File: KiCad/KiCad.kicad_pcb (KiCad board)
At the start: 2 copper layers, 74.9 x 58.4 mm, 16 parts, among them M1 Servo (SG90), U1 ESP32-DEVKITC, U2 microSD-DIP-KIT

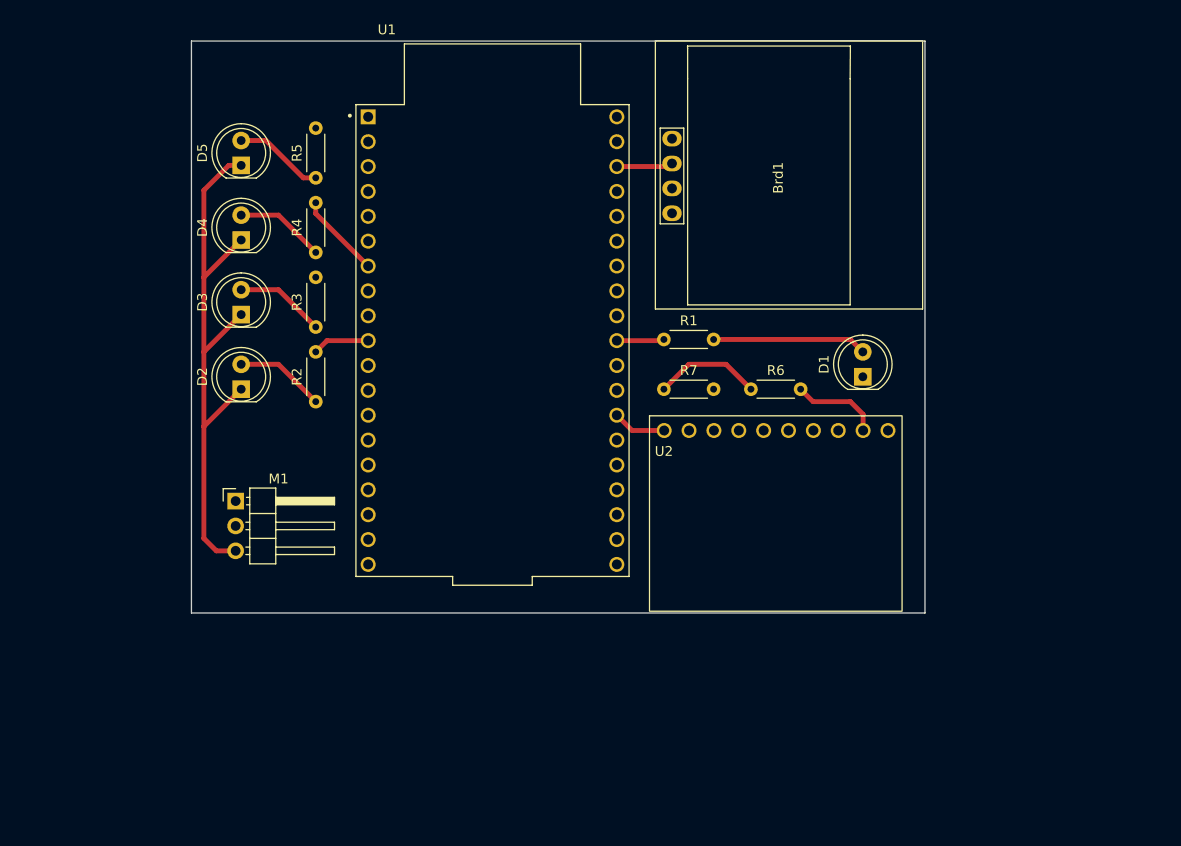
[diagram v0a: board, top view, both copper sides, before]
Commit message: KiCadの回路図追加
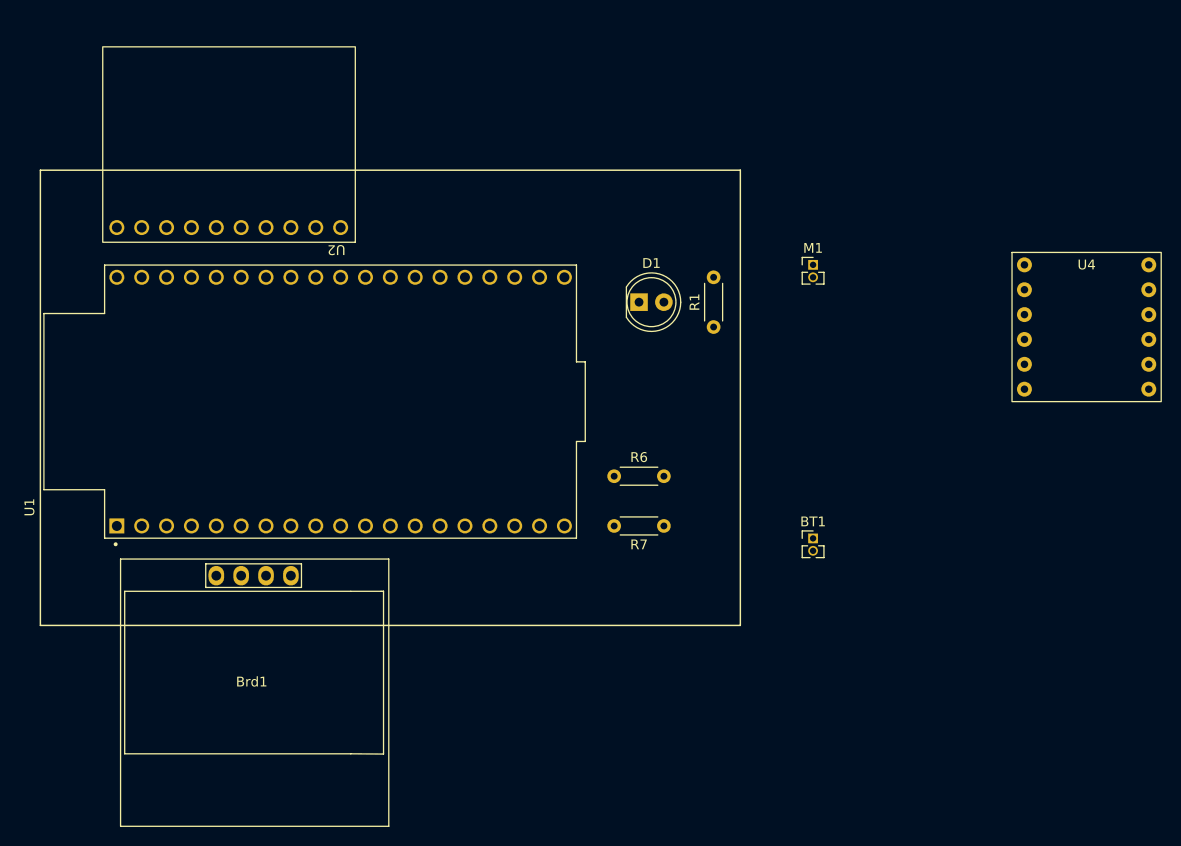
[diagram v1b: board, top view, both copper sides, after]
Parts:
- removed D2, D3, D4, D5: LED, LED_THT:LED_D5.0mm
- removed R2, R3, R4, R5: 330, Resistor_THT:R_Axial_DIN0204_L3.6mm_D1.6mm_P5.08mm_Horizontal
- added BT1: 3V (1.5V x 2), Connector_PinHeader_1.27mm:PinHeader_1x02_P1.27mm_Vertical, F.Cu at (157.5, 108.0)
- added U4: BD65496MUV, SWITCH_SCIENCE:BD65496MUV, F.Cu at (185.4, 86.4)
- D1: value Wi-Fi LED -> Wi-Fi Connecting LED
- M1: value Servo (SG90) -> FA-130; footprint Connector_PinHeader_2.54mm:PinHeader_1x03_P2.54mm_Horizontal -> Connector_PinHeader_1.27mm:PinHeader_1x02_P1.27mm_Vertical
- moved Brd1 74.1 mm to (100.1, 122.4), turned to 0 degrees
- moved M1 63.7 mm to (157.5, 80.0)
- moved U2 58.8 mm to (97.8, 77.5), turned to 180 degrees
- moved D1 24.1 mm to (139.7, 83.8), turned to 0 degrees
- moved U1 16.7 mm to (109.2, 94.0), turned to 90 degrees
- moved R6 16.6 mm to (137.2, 101.6)
- moved R7 14.0 mm to (142.2, 106.7), turned to 180 degrees
- moved R1 5.24 mm to (147.3, 86.4), turned to 90 degrees
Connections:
- Brd1 pad 2: +3.3V -> Net-(Brd1-VCC)
- M1 pad 1: Net-(M1-PWM) -> Net-(M1-+)
- M1 pad 2: +3.3V -> Net-(M1--)
- R6 pad 1: +3.3V -> Net-(Brd1-VCC)
- R7 pad 1: +3.3V -> Net-(Brd1-VCC)
- U1 pad 1: +3.3V -> Net-(Brd1-VCC)
- U1 pad 10: Net-(U1-IO26) -> unconnected-(U1-IO26-Pad10)
- U1 pad 11: Net-(U1-IO27) -> unconnected-(U1-IO27-Pad11)
- U1 pad 13: Net-(M1-PWM) -> Net-(U1-IO12)
- U1 pad 15: unconnected-(U1-IO13-Pad15) -> Net-(U1-IO13)
- U1 pad 19: unconnected-(U1-EXT_5V-Pad19) -> 5V
- U1 pad 7: Net-(U1-IO32) -> unconnected-(U1-IO32-Pad7)
- U1 pad 8: Net-(U1-IO33) -> unconnected-(U1-IO33-Pad8)
- U2 pad 4: +3.3V -> Net-(Brd1-VCC)
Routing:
- net GND: track 60.4 -> 0.00 mm
- net Net-(D1-A): track 15.8 -> 0.00 mm
- net +3.3V: track 11.0 -> 0.00 mm
- net Net-(D5-A): track 9.20 -> 0.00 mm
- net Net-(D3-A): track 9.20 -> 0.00 mm
- net Net-(D2-A): track 9.20 -> 0.00 mm
- net Net-(D4-A): track 9.20 -> 0.00 mm
- net Net-(U1-IO16): track 9.09 -> 0.00 mm
- net Net-(U1-IO32): track 8.69 -> 0.00 mm
- net Net-(U1-IO26): track 5.83 -> 0.00 mm
- net Net-(Brd1-SCL): track 5.77 -> 0.00 mm
- net Net-(U1-IO4): track 5.48 -> 0.00 mm
- net Net-(U1-IO5): track 4.86 -> 0.00 mm
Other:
- board outline removed

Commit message: ミスった
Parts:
- moved Brd1 77.6 mm to (157.1, 69.7)
- moved U2 59.5 mm to (156.6, 86.1), turned to 0 degrees
- moved U4 44.2 mm to (151.3, 114.5)
- moved D1 41.4 mm to (115.6, 117.5)
- moved M1 38.4 mm to (165.7, 117.5)
- moved R6 25.6 mm to (161.0, 111.1)
- moved R1 25.5 mm to (161.0, 107.9), turned to 0 degrees
- moved R7 20.2 mm to (161.0, 114.2), turned to 0 degrees
- moved U1 20.2 mm to (128.4, 87.9), turned to 0 degrees
- moved BT1 10.4 mm to (161.6, 117.5)
